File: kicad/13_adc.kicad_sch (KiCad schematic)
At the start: 0 parts

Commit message: Schematic complete: ethernet, emmc and adc sheets
- 09 ethernet: KSZ9031RNX with the Agilex 5 values and straps, RGMII 22R series,
  ferrite-fed analog rails, magjack J9, jack LED via 74LVC1G06
- 10 emmc: KIOXIA THGAMVG7T13BAIL, 47k pulls, CLK 10R, VCC 3V3 / VCCQ 1V8
- 13 adc: Agilex 3 card front end (SN74LV4051A, OPA365, 33R + 680p C0G,
  ADS7056 with DVDD 1V8), rail monitors on the mux
- attach/series_r/pull_r sheet helpers; STATUS.md updated

ERC: only the two known notes; all 92 pin-plan signals reach their loads.

Co-Authored-By: Claude Opus 5.5 <noreply@anthropic.com>
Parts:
- added C1301, C1306: 1u, Capacitor_SMD:C_0402_1005Metric, symbol ti135_card:C
- added C1302: 680p C0G, Capacitor_SMD:C_0402_1005Metric, symbol ti135_card:C
- added C1303, C1305: 100n, Capacitor_SMD:C_0402_1005Metric, symbol ti135_card:C
- added C1304: 4u7, Capacitor_SMD:C_0603_1608Metric, symbol ti135_card:C
- added R1301: 100R, Resistor_SMD:R_0402_1005Metric, symbol ti135_card:R
- added R1302, R1303, R1304, R1305: 1k, Resistor_SMD:R_0402_1005Metric, symbol ti135_card:R
- added R1306, R1310, R1311, R1312: 33R, Resistor_SMD:R_0402_1005Metric, symbol ti135_card:R
- added U1301: SN74LV4051APWR, Package_SO:TSSOP-16_4.4x5mm_P0.65mm, symbol ti135_card:CD4051B
- added U1302: OPA365AIDBVR, Package_TO_SOT_SMD:SOT-23-5, symbol ti135_card:OPA365xxDBV
- added U1303: ADS7056IRUGR, ti135_card:ads7056, symbol ti135_card:ADS7056
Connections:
- new net: R1306.1, U1302.1, U1302.4 (-)
- new net 1V1: R1304.1
- new net 1V8: C1306.1, R1302.1, U1303.4 (DVDD)
- new net 3V3: R1303.1
- new net 3V3_analog: C1301.1, C1303.1, C1304.1, C1305.1, U1301.16 (VDD), U1302.5 (V+), U1303.6 (AVDD)
- new net GND: C1301.2, C1302.2, C1303.2, C1304.2, C1305.2, C1306.2, R1305.2, U1301.13 (X0), U1301.6 (INH), U1301.7 (VEE), U1301.8 (VSS), U1302.2 (V-), U1303.5 (GND), U1303.8 (AINM)
- new net VCORE: R1301.1
- new net adbsel0_3v3: U1301.11 (A)
- new net adbsel1_3v3: U1301.10 (B)
- new net adbsel2_3v3: U1301.9 (C)
- new net adc_ainp: C1302.1, R1306.2, U1303.7 (AINP)
- new net adc_cs_n: R1310.1
- new net adc_cs_n_r: R1310.2, U1303.1 (~{CS})
- new net adc_mux_out: U1301.3 (X), U1302.3 (+)
- new net adc_sclk: R1311.1
- new net adc_sclk_r: R1311.2, U1303.3 (SCLK)
- new net adc_sdo: R1312.1
- new net adc_sdo_r: R1312.2, U1303.2 (SDO)
- new net isoada1: U1301.4 (X7)
- new net isoada2: U1301.1 (X4)
- new net isoada3: U1301.2 (X6)
- new net mon_1v1: R1304.2, U1301.5 (X5)
- new net mon_1v8: R1302.2, U1301.15 (X2)
- new net mon_3v3: R1303.2, R1305.1, U1301.12 (X3)
- new net mon_vcore: R1301.2, U1301.14 (X1)
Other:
- note added: "3V3 via 1k/1k divider"
- note added: "ADC chain: mux U1301 -> buffer U1302 -> ADS7056 U1303 (front end as on the Agilex 3 card, 2.5 MSPS design). Mux: X0 GND (zero ref), X1 VCORE, X2 1V8, X3 3V3/2, X4 isoada2, X5 1V1, X6 isoada3, X7 isoada1. Full scale 0..3.3 V (AVDD = reference). The FPGA maps the channel numbers."
- note added: "AVDD = reference: 4u7 0603 + 100n at the pin"
- note added: "DVDD 1V8"
- note added: "Rail monitors"
- note added: "SPI series 33 R (60 MHz SCLK)"
- note added: "U1301 VDD"
- note added: "U1302 V+"

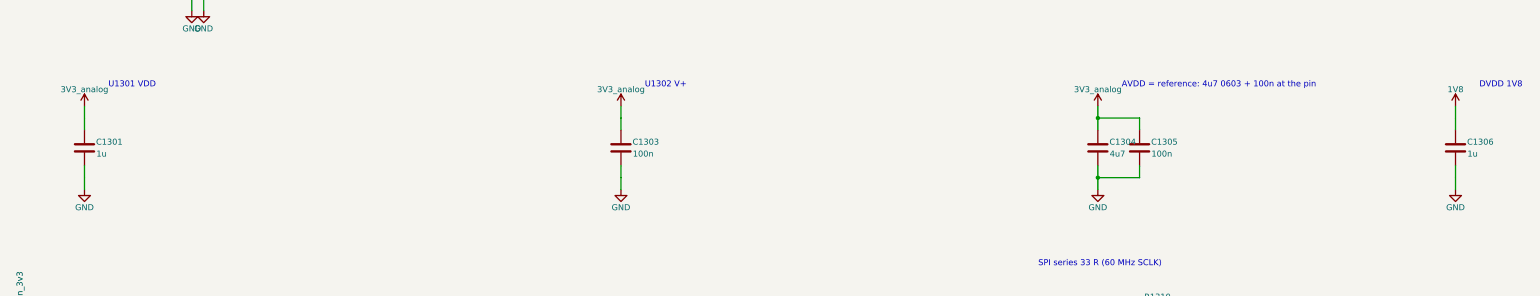
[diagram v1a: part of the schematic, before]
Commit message: LPDDR4 hand routing: Agilex DRAM escape copied, byte lanes routed, DQ swizzle by hand
- U801 decoupling = the Agilex U12 set (sheet 08: 29 x 100n 0201, 22u/1u 0402, LCSC from the
  Agilex card), placed at the Agilex positions on the same via pairs; R802 (ZQ) at R43's spot;
  CA/CKE T-branches on B.Cu copied (tools/ddr/copy_dram_escape.py)
- LPDDR4 vias not on a BGA ball removed (T-branch centre vias kept)
- Schematic: #PWR/#FLG references made unique per sheet (prefix = sheet number); the
  duplicates blocked Update PCB from Schematic
- DQ swizzle now edited by hand in the schematic (bytes 0 and 2); efinity/pinplan/lpddr4_swizzle.json
  is not updated yet
- Byte lanes routed by hand (work in progress)

Known open (WIP): byte 2 - ddr_dq22 on two U501 balls (AA16, W16), ddr_dq21 has no U501 ball;
DRC shows 2 shorts at U501 Y16/W16 (dq21/dq17 tracks).

Co-Authored-By: Claude Opus 5.5 <noreply@anthropic.com>
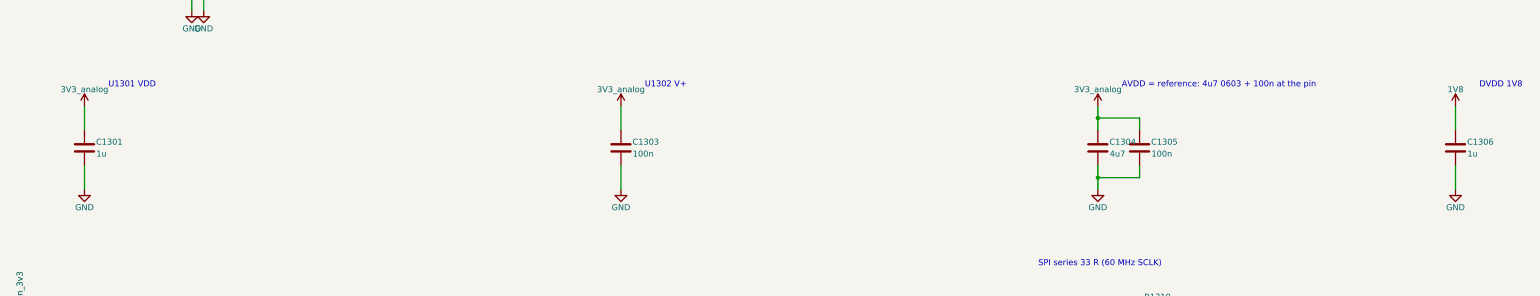
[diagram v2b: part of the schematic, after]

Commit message: LCSC numbers for all JLC parts; Y701 -> YXC OT322525MJBA4SL
- tools/set_lcsc.py: one table (value, footprint) -> LCSC, fills empty LCSC fields in the
  sheets; 312 symbols. JLC basic parts where available, cap voltages checked per rail,
  VCORE divider 0.1 % (no 0.5 % in stock). Board fields synced with add_parts.py.
- Y701: the SiT8924 has no JLC stock; now YXC OT322525MJBA4SL (C669088, 3225), EN tied
  to 1V8. R701/C701 moved 0.5 mm to clear its courtyard. Netlist change: Y701 pin 1 -> 1V8.
- Only U501 (Ti135) is left without LCSC (global sourcing / consigned).
- DRC: schematic parity 0.

Co-Authored-By: Claude Opus 5.5 <noreply@anthropic.com>
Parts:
- C1301, C1306: LCSC (none) -> C52923
- C1302: LCSC (none) -> C126514
- C1303, C1305: LCSC (none) -> C1525
- C1304: LCSC (none) -> C19666
- R1301: LCSC (none) -> C25076
- R1302, R1303, R1304, R1305: LCSC (none) -> C11702
- R1306, R1310, R1311, R1312: LCSC (none) -> C25105
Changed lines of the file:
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@@
 			)
 		)
+		(property "LCSC" "C25105"
+			(at 304.8 194.31 0)
+			(effects
+				(font
+					(size 1.27 1.27)
+				)
+				(hide yes)
+			)
+		)
 		(pin "1"
 		)
@@
 			)
 		)
+		(property "LCSC" "C52923"
+			(at 368.3 152.4 0)
+			(effects
+				(font
+					(size 1.27 1.27)
+				)
+				(hide yes)
+			)
+		)
 		(pin "1"
 		)
@@
 			)
 		)
+		(property "LCSC" "C1525"
+			(at 190.5 152.4 0)
+			(effects
+				(font
+					(size 1.27 1.27)
+				)
+				(hide yes)
+			)
+		)
 		(pin "1"
 		)
@@
 			)
 		)
+		(property "LCSC" "C11702"
+			(at 43.18 193.04 0)
+			(effects
+				(font
+					(size 1.27 1.27)
+				)
+				(hide yes)
+			)
+		)
 		(pin "1"
 		)
@@
 			)
 		)
+		(property "LCSC" "C25105"
+			(at 223.52 101.6 0)
+			(effects
+				(font
+					(size 1.27 1.27)
+				)
+				(hide yes)
+			)
+		)
 		(pin "1"
 		)
@@
 			)
 		)
+		(property "LCSC" "C126514"
+			(at 232.41 107.95 0)
+			(effects
+				(font
+					(size 1.27 1.27)
+				)
+				(hide yes)
+			)
+		)
 		(pin "1"
 		)
@@
 			)
 		)
+		(property "LCSC" "C25076"
+			(at 22.86 193.04 0)
+			(effects
+				(font
+					(size 1.27 1.27)
+				)
+				(hide yes)
+			)
+		)
 		(pin "1"
 		)
@@
 			)
 		)
+		(property "LCSC" "C11702"
+			(at 63.5 193.04 0)
+			(effects
+				(font
+					(size 1.27 1.27)
+				)
+				(hide yes)
+			)
+		)
 		(pin "1"
 		)
@@
 			)
 		)
+		(property "LCSC" "C52923"
+			(at 76.2 152.4 0)
+			(effects
+				(font
+					(size 1.27 1.27)
+				)
+				(hide yes)
+			)
+		)
 		(pin "1"
 		)
@@
 			)
 		)
+		(property "LCSC" "C11702"
+			(at 33.02 193.04 0)
+			(effects
+				(font
+					(size 1.27 1.27)
+				)
+				(hide yes)
+			)
+		)
 		(pin "1"
 		)
@@
 			)
 		)
+		(property "LCSC" "C11702"
+			(at 53.34 193.04 0)
+			(effects
+				(font
+					(size 1.27 1.27)
+				)
+				(hide yes)
+			)
+		)
 		(pin "1"
 		)
@@
 			)
 		)
+		(property "LCSC" "C1525"
+			(at 300.99 152.4 0)
+			(effects
+				(font
+					(size 1.27 1.27)
+				)
+				(hide yes)
+			)
+		)
 		(pin "1"
 		)
@@
 			)
 		)
+		(property "LCSC" "C25105"
+			(at 304.8 200.66 0)
+			(effects
+				(font
+					(size 1.27 1.27)
+				)
+				(hide yes)
+			)
+		)
 		(pin "1"
 		)
@@
 			)
 		)
+		(property "LCSC" "C25105"
+			(at 304.8 187.96 0)
+			(effects
+				(font
+					(size 1.27 1.27)
+				)
+				(hide yes)
+			)
+		)
 		(pin "1"
 		)
@@
 			)
 		)
+		(property "LCSC" "C19666"
+			(at 292.1 152.4 0)
+			(effects
+				(font
+					(size 1.27 1.27)
+				)
+				(hide yes)
+			)
+		)

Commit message: ADC: buffer isoada1..3 before the mux (OPA365 followers)
The baseboard now filters ISOADA1/2 with 8.2k + 4.7n and ISOADA3 with 8.2k + 10n. Fed straight into the
SN74LV4051A, that source had to recharge the ~30 pF mux common node after every channel switch
(tau 39/82 us), leaving a crosstalk error of about 8.2k x f_switch x 30 pF x dV.

Each input now runs J3 -> 1k -> OPA365AIDBVR follower (U1304..U1306) -> mux, with 1n C0G to card GND at
the + input (159 kHz, filters the ground difference across J3) and 100n decoupling. The mux labels are
isoadaN_buf; the sheet pins keep their names. 1n C0G (C76947) added to set_lcsc.py.

Co-Authored-By: Claude Opus 5.5 <noreply@anthropic.com>
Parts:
- added C1307, C1308, C1309: 1n C0G, Capacitor_SMD:C_0402_1005Metric, symbol ti135_card:C
- added C1310, C1311, C1312: 100n, Capacitor_SMD:C_0402_1005Metric, symbol ti135_card:C
- added R1307, R1308, R1309: 1k, Resistor_SMD:R_0402_1005Metric, symbol ti135_card:R
- added U1304, U1305, U1306: OPA365AIDBVR, Package_TO_SOT_SMD:SOT-23-5, symbol ti135_card:OPA365xxDBV
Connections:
- net 3V3_analog: now also C1310.1, C1311.1, C1312.1, U1304.5 (V+), U1305.5 (V+), U1306.5 (V+)
- net GND: now also C1307.2, C1308.2, C1309.2, C1310.2, C1311.2, C1312.2, U1304.2 (V-), U1305.2 (V-), U1306.2 (V-)
- net isoada1: now also R1307.1; no longer U1301.4 (X7)
- net isoada2: now also R1308.1; no longer U1301.1 (X4)
- net isoada3: now also R1309.1; no longer U1301.2 (X6)
- new net: C1309.1, R1309.2, U1306.3 (+)
- new net: C1308.1, R1308.2, U1305.3 (+)
- new net: C1307.1, R1307.2, U1304.3 (+)
- new net isoada1_buf: U1301.4 (X7), U1304.1, U1304.4 (-)
- new net isoada2_buf: U1301.1 (X4), U1305.1, U1305.4 (-)
- new net isoada3_buf: U1301.2 (X6), U1306.1, U1306.4 (-)
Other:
- note added: "ADC chain: mux U1301 -> buffer U1302 -> ADS7056 U1303 (front end as on the Agilex 3 card, 2.5 MSPS design). Mux: X0 GND (zero ref), X1 VCORE, X2 1V8, X3 3V3/2, X4 isoada2, X5 1V1, X6 isoada3, X7 isoada1 (isoada1..3 buffered by U1304..U1306 before the mux). Full scale 0..3.3 V (AVDD = reference). The FPGA maps the channel numbers."
- note added: "J3 isoada buffers: the mux common node (~30 pF) never loads the baseboard's 8.2k + 4.7n/10n source; 1k + 1n C0G to card GND filters the ground difference across J3"
- note removed: "ADC chain: mux U1301 -> buffer U1302 -> ADS7056 U1303 (front end as on the Agilex 3 card, 2.5 MSPS design). Mux: X0 GND (zero ref), X1 VCORE, X2 1V8, X3 3V3/2, X4 isoada2, X5 1V1, X6 isoada3, X7 isoada1. Full scale 0..3.3 V (AVDD = reference). The FPGA maps the channel numbers."
